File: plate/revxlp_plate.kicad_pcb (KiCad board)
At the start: 2 copper layers, 238.7 x 87.9 mm, 2 parts

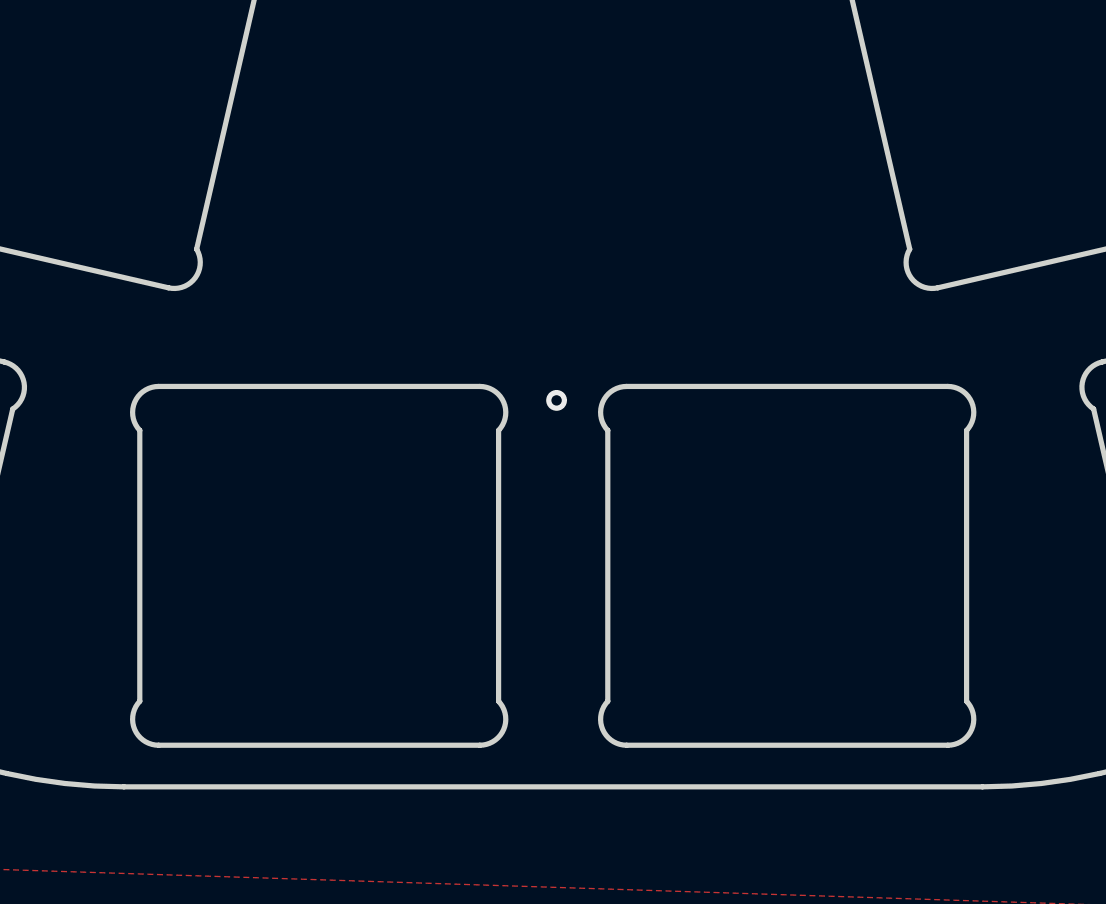
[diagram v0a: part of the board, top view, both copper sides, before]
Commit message: Add JST socket, various tweaks/fixes.
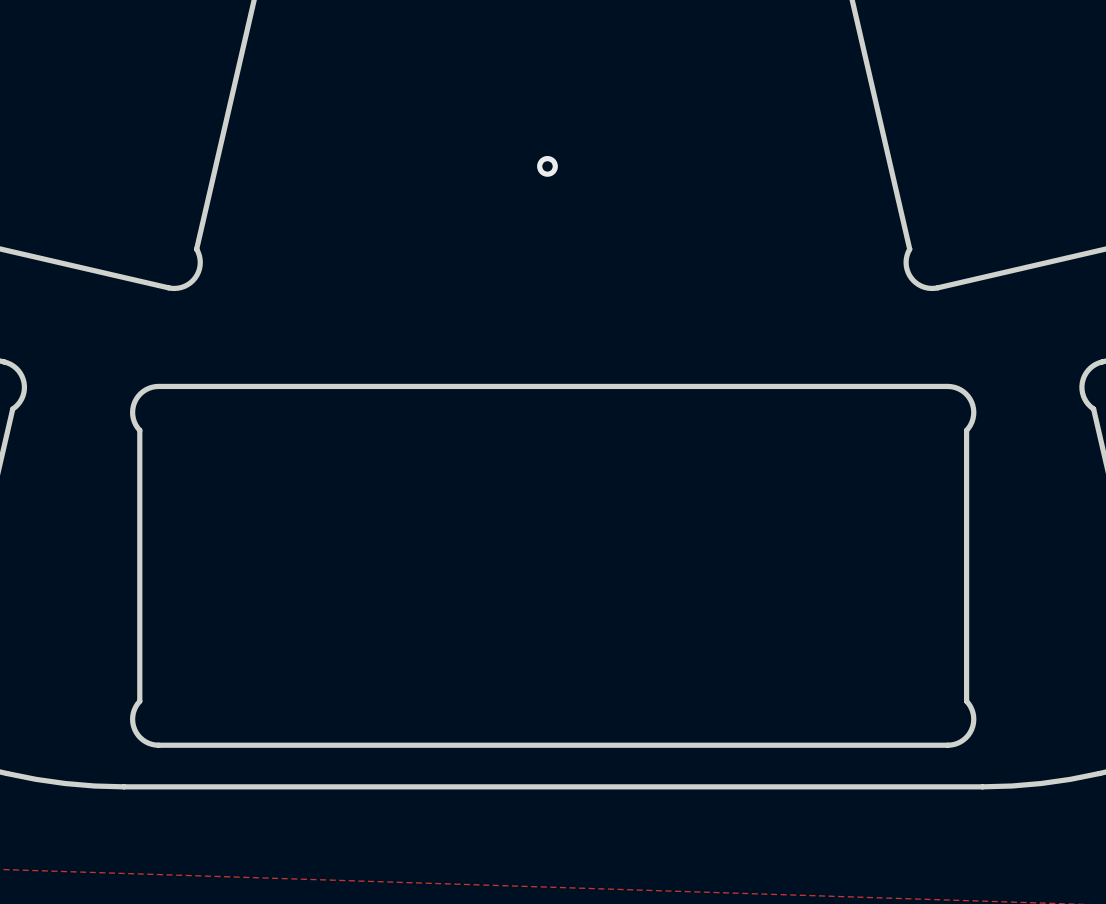
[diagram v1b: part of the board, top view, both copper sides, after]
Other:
- outline, holes or cut-outs redrawn
